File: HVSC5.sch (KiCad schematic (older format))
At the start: 8 parts

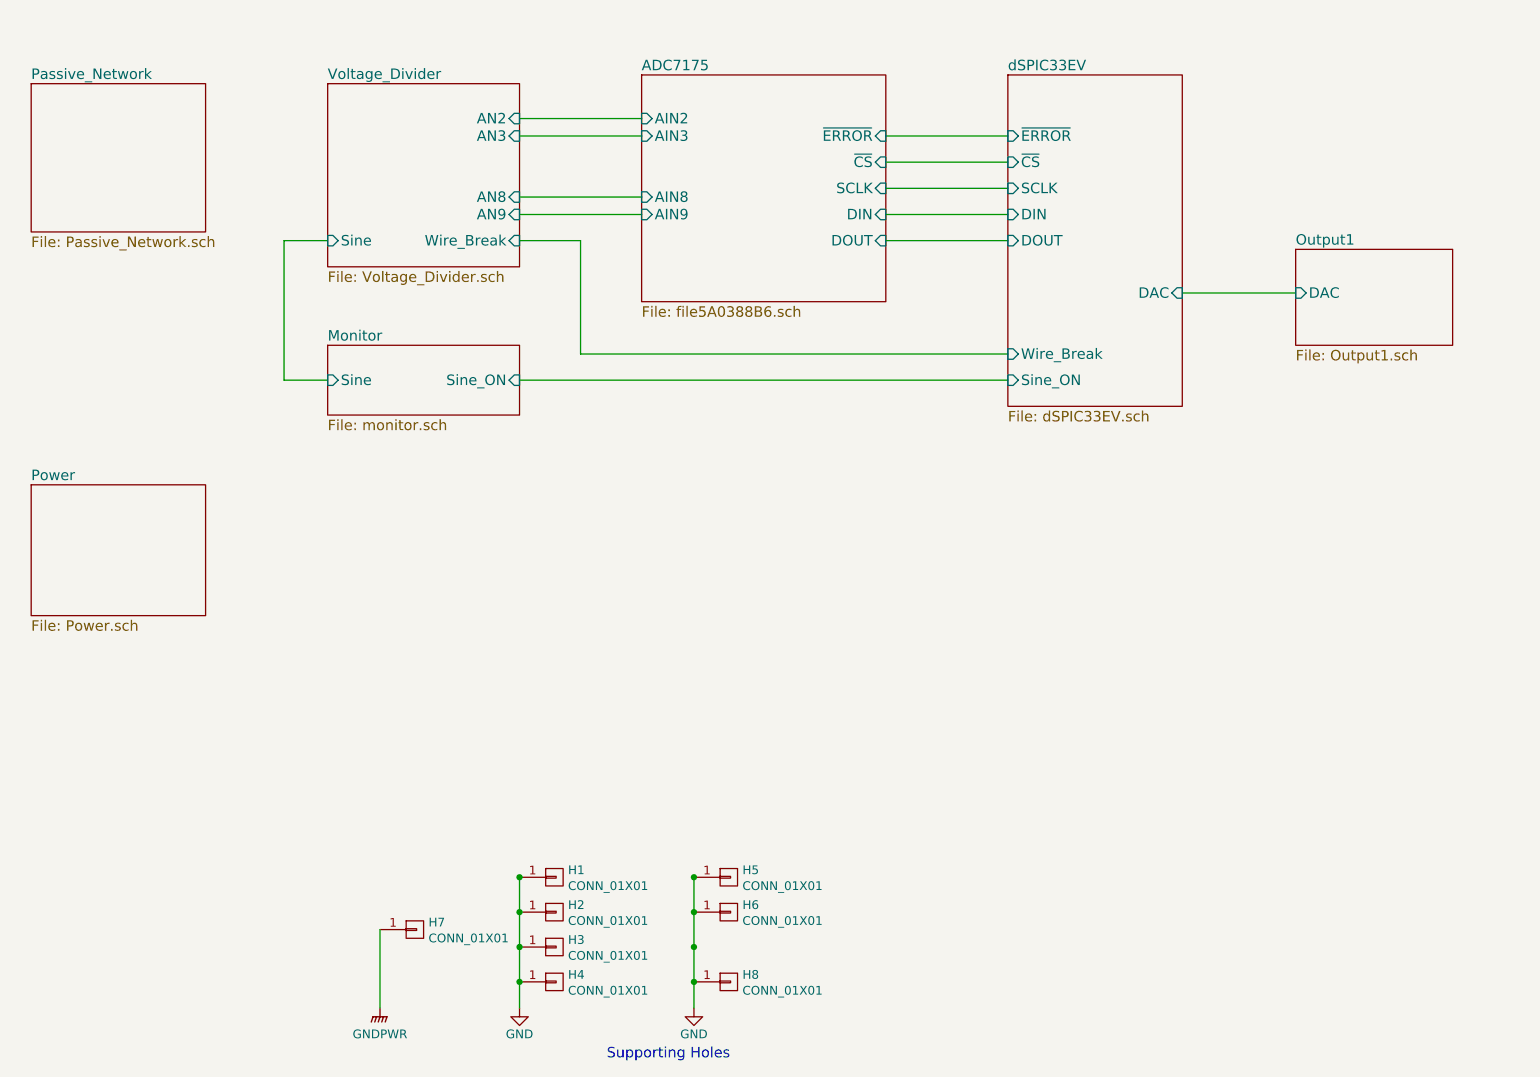
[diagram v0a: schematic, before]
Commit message: Soldering sequence
솔더링 순서
1st CPU PW ADC
2nd Filter
3rd DAC out
4th Sine generator
5th Voltage divider & protection
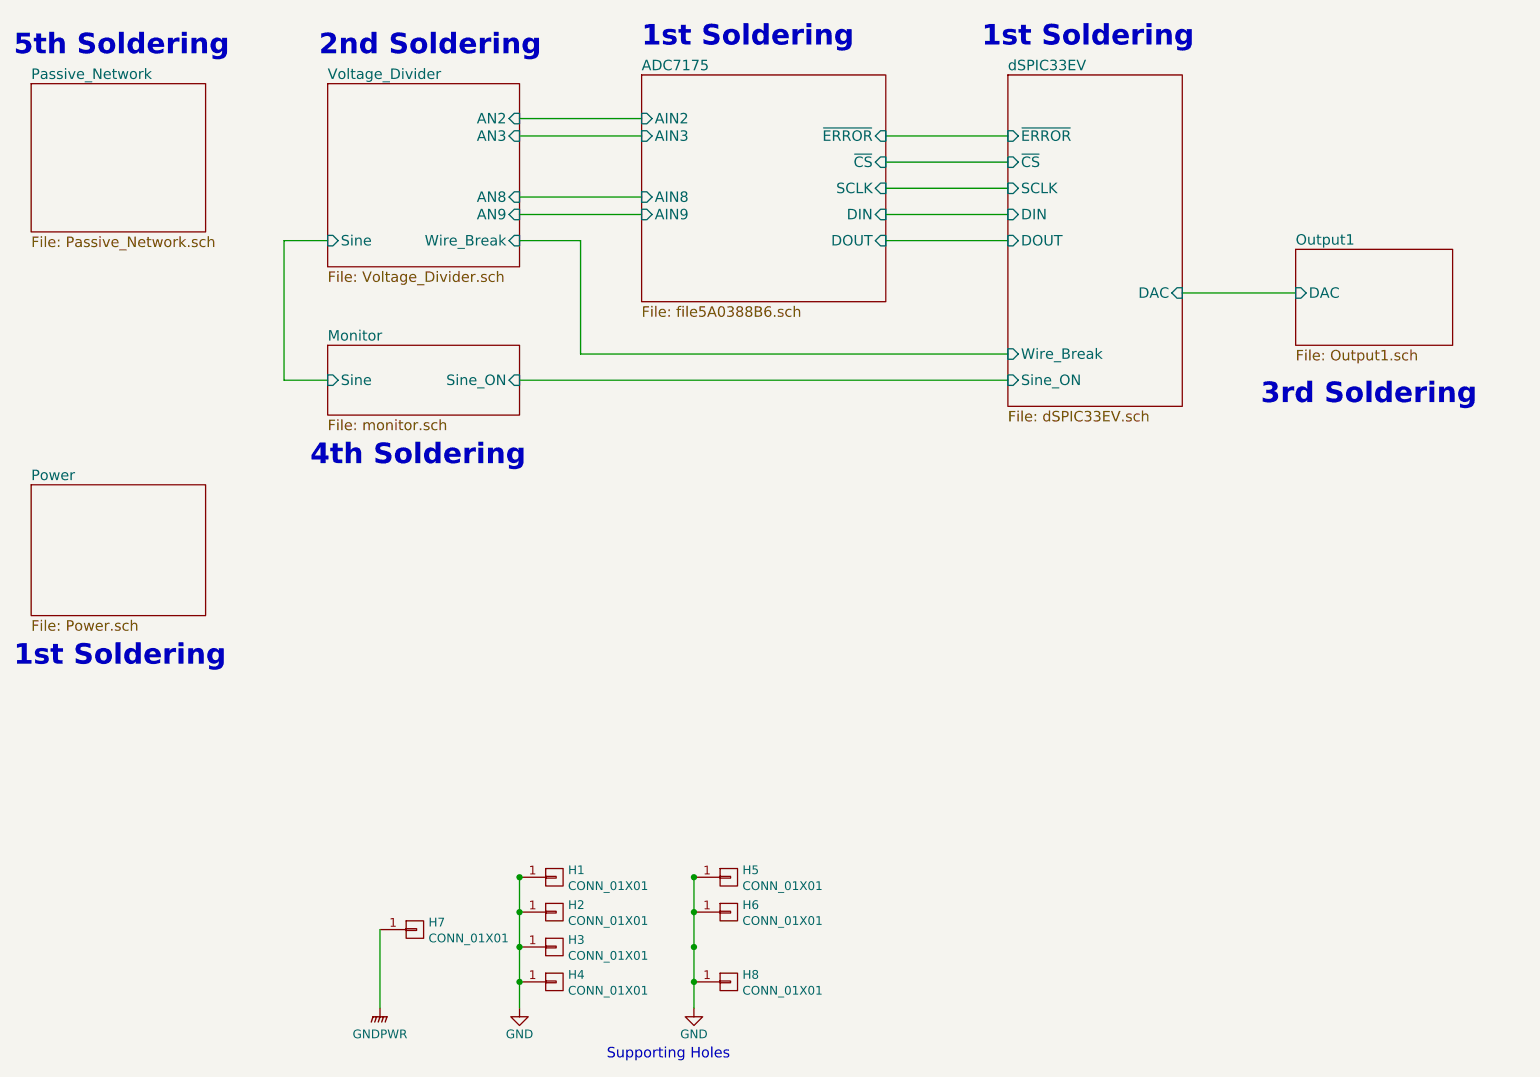
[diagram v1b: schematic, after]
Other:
- note added: "1st Soldering"
- note added: "2nd Soldering"
- note added: "3rd Soldering"
- note added: "4th Soldering"
- note added: "5th Soldering"
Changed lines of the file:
@@
 	1    0    0    -1
 $EndComp
+Text Notes 7600 1850 0    118  ~ 24
+1st Soldering
+Text Notes 5650 1850 0    118  ~ 24
+1st Soldering
+Text Notes 2050 5400 0    118  ~ 24
+1st Soldering
+Text Notes 3800 1900 0    118  ~ 24
+2nd Soldering
+Text Notes 9200 3900 0    118  ~ 24
+3rd Soldering
+Text Notes 3750 4250 0    118  ~ 24
+4th Soldering
+Text Notes 2050 1900 0    118  ~ 24
+5th Soldering
 $EndSCHEMATC

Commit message: 2차PCB
U22 포함
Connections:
- net GND: no longer H1.1 (P1), H3.1 (P1), H4.1 (P1), H5.1 (P1)
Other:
- moved on the sheet: H1, H2, H3, H4, H5
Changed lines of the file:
@@
 L CONN_01X01 H5
 U 1 1 5ABEE9AA
-P 6150 6600
-F 0 "H5" H 6228 6641 50  0000 L CNN
-F 1 "CONN_01X01" H 6228 6550 50  0000 L CNN
-F 2 "Mounting_Holes:MountingHole_3.2mm_M3_Pad_Via" H 6150 6600 50  0001 C CNN
-F 3 "" H 6150 6600 50  0001 C CNN
-	1    6150 6600
+P 5250 6800
+F 0 "H5" H 5328 6841 50  0000 L CNN
+F 1 "CONN_01X01" H 5328 6750 50  0000 L CNN
+F 2 "Mounting_Holes:MountingHole_3.2mm_M3_Pad_Via" H 5250 6800 50  0001 C CNN
+F 3 "" H 5250 6800 50  0001 C CNN
+	1    5250 6800
 	1    0    0    -1
 $EndComp
@@
 L CONN_01X01 H2
 U 1 1 5ABEE9C5
-P 5150 6800
-F 0 "H2" H 5228 6841 50  0000 L CNN
-F 1 "CONN_01X01" H 5228 6750 50  0000 L CNN
-F 2 "Mounting_Holes:MountingHole_3.2mm_M3_Pad_Via" H 5150 6800 50  0001 C CNN
-F 3 "" H 5150 6800 50  0001 C CNN
-	1    5150 6800
+P 6150 7000
+F 0 "H2" H 6228 7041 50  0000 L CNN
+F 1 "CONN_01X01" H 6228 6950 50  0000 L CNN
+F 2 "Mounting_Holes:MountingHole_3.2mm_M3_Pad_Via" H 6150 7000 50  0001 C CNN
+F 3 "" H 6150 7000 50  0001 C CNN
+	1    6150 7000
 	1    0    0    -1
 $EndComp
@@
 L CONN_01X01 H1
 U 1 1 5ABEE9CC
-P 5150 6600
-F 0 "H1" H 5228 6641 50  0000 L CNN
-F 1 "CONN_01X01" H 5228 6550 50  0000 L CNN
-F 2 "Mounting_Holes:MountingHole_3.2mm_M3_Pad_Via" H 5150 6600 50  0001 C CNN
-F 3 "" H 5150 6600 50  0001 C CNN
-	1    5150 6600
+P 5250 6600
+F 0 "H1" H 5328 6641 50  0000 L CNN
+F 1 "CONN_01X01" H 5328 6550 50  0000 L CNN
+F 2 "Mounting_Holes:MountingHole_3.2mm_M3_Pad_Via" H 5250 6600 50  0001 C CNN
+F 3 "" H 5250 6600 50  0001 C CNN
+	1    5250 6600
 	1    0    0    -1
 $EndComp
@@
 L CONN_01X01 H4
 U 1 1 5ABEE9D3
-P 5150 7200
-F 0 "H4" H 5228 7241 50  0000 L CNN
-F 1 "CONN_01X01" H 5228 7150 50  0000 L CNN
-F 2 "Mounting_Holes:MountingHole_3.2mm_M3_Pad_Via" H 5150 7200 50  0001 C CNN
-F 3 "" H 5150 7200 50  0001 C CNN
-	1    5150 7200
+P 5250 7200
+F 0 "H4" H 5328 7241 50  0000 L CNN
+F 1 "CONN_01X01" H 5328 7150 50  0000 L CNN
+F 2 "Mounting_Holes:MountingHole_3.2mm_M3_Pad_Via" H 5250 7200 50  0001 C CNN
+F 3 "" H 5250 7200 50  0001 C CNN
+	1    5250 7200
 	1    0    0    -1
 $EndComp
@@
 L CONN_01X01 H3
 U 1 1 5ABEE9DA
-P 5150 7000
-F 0 "H3" H 5228 7041 50  0000 L CNN
-F 1 "CONN_01X01" H 5228 6950 50  0000 L CNN
-F 2 "Mounting_Holes:MountingHole_3.2mm_M3_Pad_Via" H 5150 7000 50  0001 C CNN
-F 3 "" H 5150 7000 50  0001 C CNN
-	1    5150 7000
+P 5250 7000
+F 0 "H3" H 5328 7041 50  0000 L CNN
+F 1 "CONN_01X01" H 5328 6950 50  0000 L CNN
+F 2 "Mounting_Holes:MountingHole_3.2mm_M3_Pad_Via" H 5250 7000 50  0001 C CNN
+F 3 "" H 5250 7000 50  0001 C CNN
+	1    5250 7000
 	1    0    0    -1
 $EndComp
-$Comp
-L GND #PWR01
-U 1 1 5ABEE9E1
-P 4950 7350
-F 0 "#PWR01" H 4950 7100 50  0001 C CNN
-F 1 "GND" H 4950 7200 50  0000 C CNN
-F 2 "" H 4950 7350 50  0001 C CNN
-F 3 "" H 4950 7350 50  0001 C CNN
-	1    4950 7350
-	1    0    0    -1
-$EndComp
-Text Notes 5450 7650 0    60   ~ 0
+Text Notes 4750 7650 0    60   ~ 0
 Supporting Holes\n
 Wire Wire Line
-	5950 6600 5950 7350
+	5950 6800 5950 7350
 Connection ~ 5950 7200
 Connection ~ 5950 7000
 Connection ~ 5950 6800
-Connection ~ 5950 6600
-Wire Wire Line
-	4950 6600 4950 7350
-Connection ~ 4950 7200
-Connection ~ 4950 7000
-Connection ~ 4950 6800
-Connection ~ 4950 6600
 $Sheet
 S 2150 2050 1000 850

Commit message: 3차 PCB
1. 모니터 고압부 150k옴 2갤로 수정
2. 6.5V Zener 추가
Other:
- note removed: "1st Soldering"
- note removed: "2nd Soldering"
- note removed: "3rd Soldering"
- note removed: "4th Soldering"
- note removed: "5th Soldering"
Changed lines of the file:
@@
 	1    0    0    -1
 $EndComp
-Text Notes 7600 1850 0    118  ~ 24
-1st Soldering
-Text Notes 5650 1850 0    118  ~ 24
-1st Soldering
-Text Notes 2050 5400 0    118  ~ 24
-1st Soldering
-Text Notes 3800 1900 0    118  ~ 24
-2nd Soldering
-Text Notes 9200 3900 0    118  ~ 24
-3rd Soldering
-Text Notes 3750 4250 0    118  ~ 24
-4th Soldering
-Text Notes 2050 1900 0    118  ~ 24
-5th Soldering
 $EndSCHEMATC

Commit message: 4차 PCB
U23 Wire Breakage Relay 추가
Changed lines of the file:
@@
 $EndDescr
 $Sheet
-S 5650 2000 1400 1300
+S 5650 2000 1400 1150
 U 5A0388B7
 F0 "ADC7175" 60
@@
 F8 "Sine_ON" I L 7750 3750 60
 F9 "Wire_Break" I L 7750 3600 60
+F10 "Sine_APP" I L 7750 3500 60
 $EndSheet
 $Sheet
@@
 $EndSheet
 $Sheet
-S 3850 2050 1100 1050
+S 3850 2050 1100 1200
 U 5B05474E
 F0 "Voltage_Divider" 60
@@
 F2 "AN2" I R 4950 2250 60
 F3 "AN3" I R 4950 2350 60
-F4 "Wire_Break" I R 4950 2950 60
+F4 "Wire_Break" I R 4950 3100 60
 F5 "Sine" I L 3850 2950 60
 F6 "AN8" I R 4950 2700 60
 F7 "AN9" I R 4950 2800 60
+F8 "Sine_APP" I R 4950 3000 60
 $EndSheet
 Wire Wire Line
@@
 	4950 2350 5650 2350
 Wire Wire Line
-	5300 2950 4950 2950
+	5300 3100 4950 3100
 Wire Wire Line
 	4950 2700 5650 2700
@@
 	5300 3600 7750 3600
 Wire Wire Line
-	5300 2950 5300 3600
+	5300 3100 5300 3600
 Wire Wire Line
 	4950 3750 7750 3750
@@
 	1    0    0    -1
 $EndComp
+Wire Wire Line
+	4950 3000 5400 3000
+Wire Wire Line
+	5400 3000 5400 3500
+Wire Wire Line
+	5400 3500 7750 3500
 $EndSCHEMATC
